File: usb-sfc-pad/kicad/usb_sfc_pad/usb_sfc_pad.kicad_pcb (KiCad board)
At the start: 2 copper layers, 36 parts, among them IC101 PIC16F1459-ISS, J101 532610671, J102 HEADER_6P-2.54, J103 532610271, J104 532610271, J105 532610271, J106 532610271, SW101 SW_Pad, SW102 SW_Pad, SW103 SW_Pad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

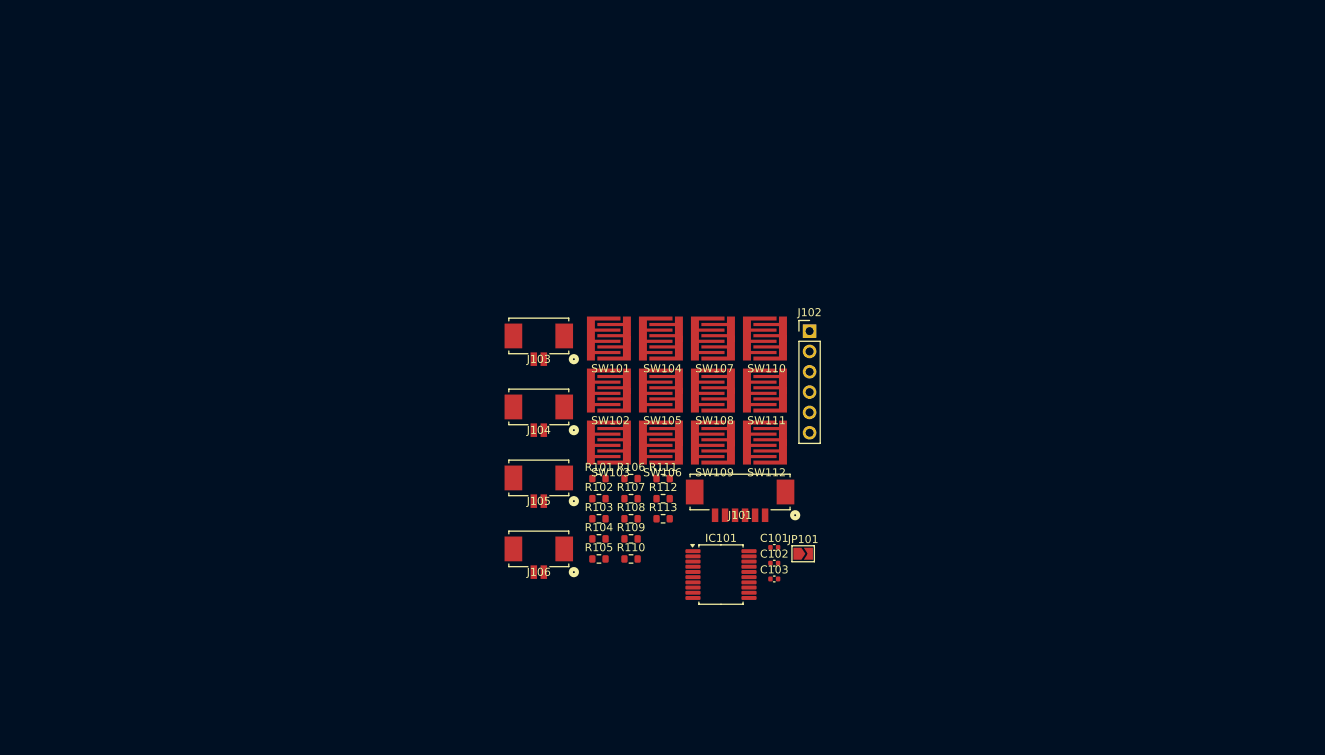
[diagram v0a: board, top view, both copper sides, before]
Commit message: Add PCB
- Renumber SFC_Pad's pins
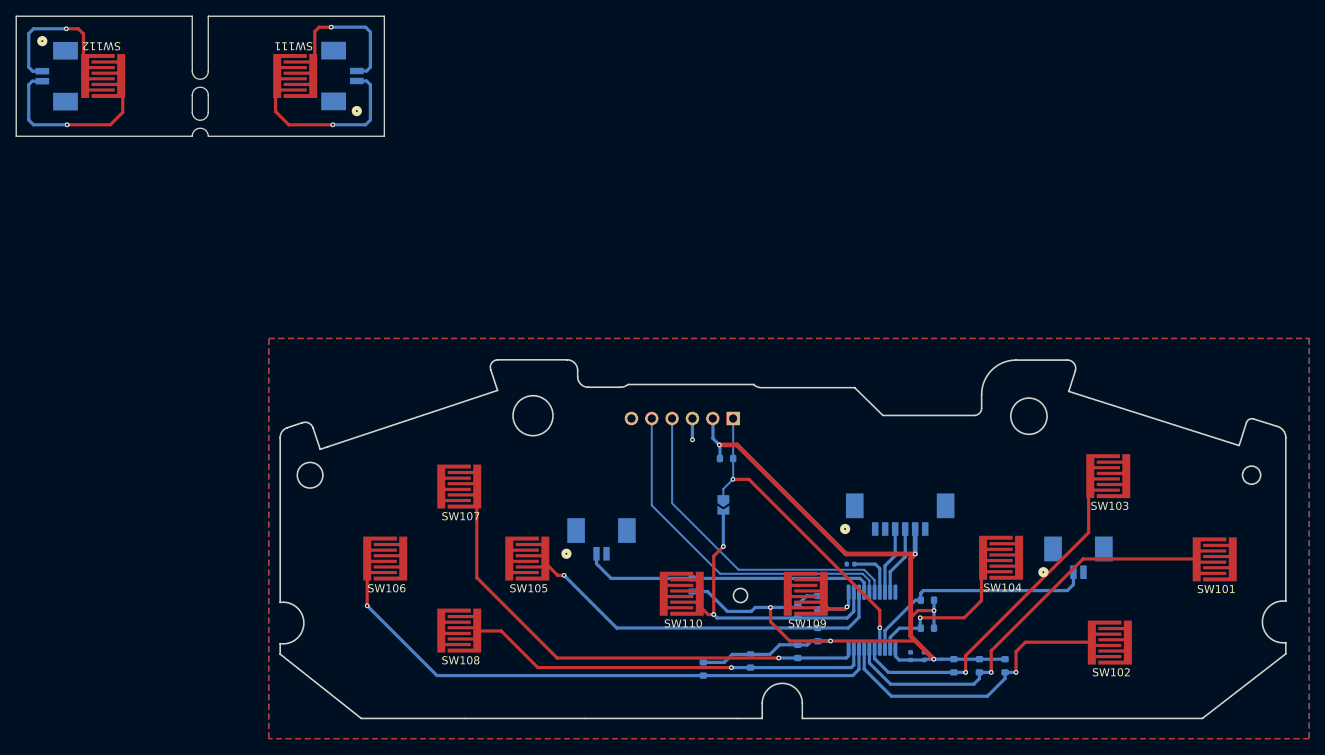
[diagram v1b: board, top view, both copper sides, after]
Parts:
- C101, C102, C103, IC101, J101, J102, J103, J104, J105, J106, JP101, R101, R102, R103, R104, R105, R106, R107, R108, R109, R110, R111, R112, R113: moved to B.Cu
- moved SW112 94.5 mm to (69.3, 47.2), turned to 180 degrees
- moved J106 83.6 mm to (64.6, 47.2), turned to 90 degrees
- moved SW101 80.6 mm to (208.2, 107.6)
- moved J103 72.5 mm to (191.2, 106.3), turned to 180 degrees
- moved SW111 70.6 mm to (93.3, 47.2), turned to 180 degrees
- moved SW102 70.1 mm to (195.1, 118.0)
- moved SW103 62.5 mm to (194.9, 97.2)
- moved R102 54.9 mm to (182.0, 120.9), turned to -90 degrees
- moved R101 53.0 mm to (178.8, 120.9), turned to -90 degrees
- moved SW104 50.6 mm to (181.5, 107.4)
- moved J104 48.7 mm to (98.1, 47.2), turned to -90 degrees
- moved R103 48.0 mm to (175.6, 120.9), turned to -90 degrees
- moved SW108 43.6 mm to (113.8, 116.5)
- moved R104 42.5 mm to (172.3, 116.2), turned to 180 degrees
- moved SW106 37.4 mm to (104.5, 107.5)
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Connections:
- IC101 pad 14: PL -> TL
- SW101 pad 1: A -> GND
- SW101 pad 2: GND -> A
- SW102 pad 1: B -> GND
- SW102 pad 2: GND -> B
- SW103 pad 1: X -> GND
- SW103 pad 2: GND -> X
- SW104 pad 1: Y -> GND
- SW104 pad 2: GND -> Y
- SW106 pad 1: LEFT -> GND
- SW106 pad 2: GND -> LEFT
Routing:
- net +5V: track 0.00 -> 133.9 mm, vias 0 -> 6
- net LEFT: track 0.00 -> 74.1 mm, vias 0 -> 1
- net UP: track 0.00 -> 63.2 mm, vias 0 -> 1
- net A: track 0.00 -> 52.2 mm, vias 0 -> 1
- net DOWN: track 0.00 -> 51.1 mm, vias 0 -> 1
- net RIGHT: track 0.00 -> 46.7 mm, vias 0 -> 1
- net X: track 0.00 -> 44.3 mm, vias 0 -> 1
- net PGC: track 0.00 -> 43.4 mm
- net PGD: track 0.00 -> 41.4 mm
- net MCLR: track 0.00 -> 40.5 mm, vias 0 -> 2
- net SELECT: track 0.00 -> 37.5 mm, vias 0 -> 2
- net B: track 0.00 -> 37.0 mm, vias 0 -> 1
- net TL: track 0.00 -> 36.9 mm
- net TR: track 0.00 -> 30.2 mm
- net Net-(J104-Pad1): track 0.00 -> 23.8 mm, vias 0 -> 1
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- added copper zone on B.Cu, net GND
- added copper zone on F.Cu, net GND
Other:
- board outline added: 158.6 x 87.8 mm

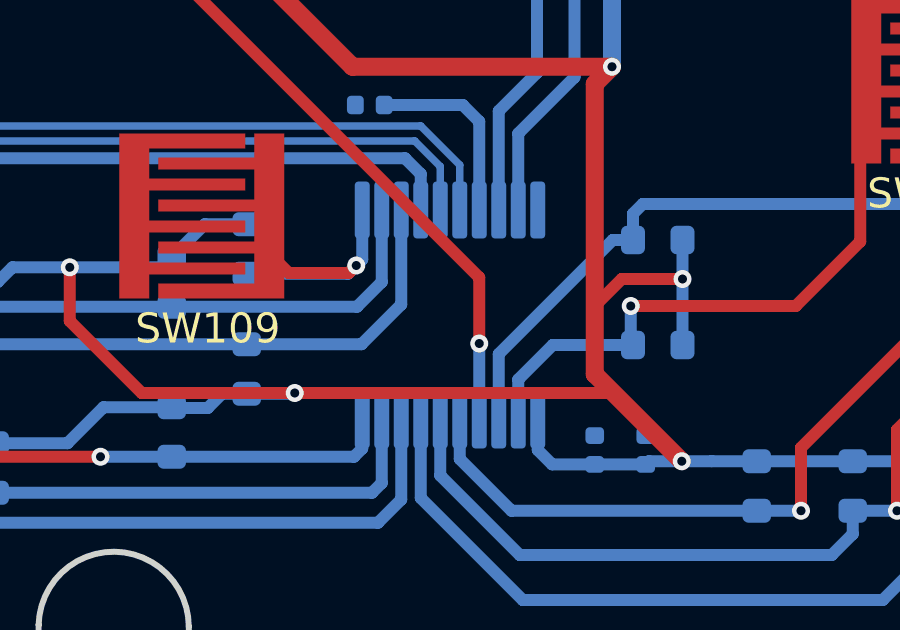
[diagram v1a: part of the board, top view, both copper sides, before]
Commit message: Fix clearance in IC101 pads
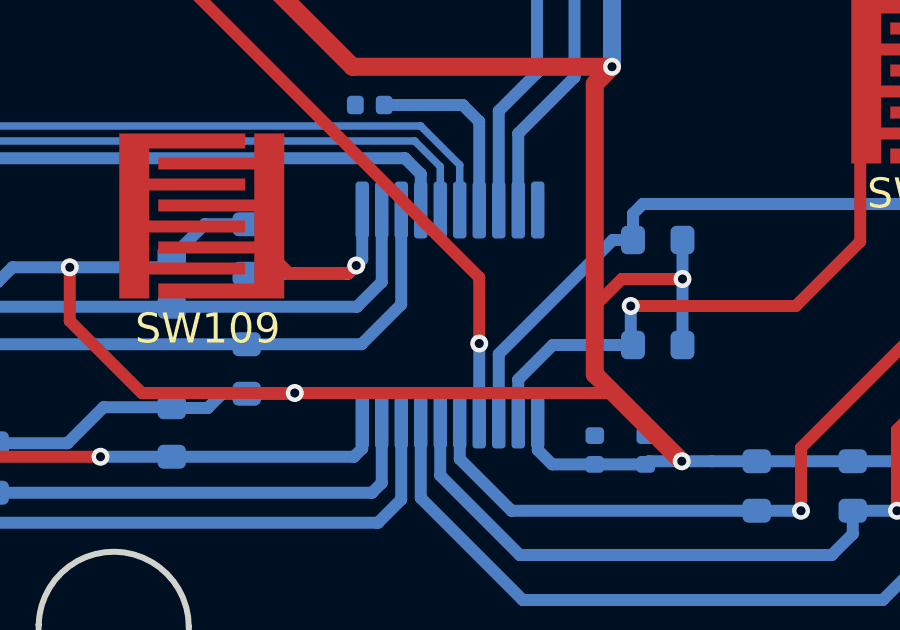
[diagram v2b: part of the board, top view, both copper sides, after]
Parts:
- IC101: footprint Package_SO:SSOP-20_5.3x7.2mm_P0.65mm -> Local:SSOP-20_5.3x7.2mm_P0.65mm
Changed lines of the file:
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@@
 		)
 	)
-	(footprint "Package_SO:SSOP-20_5.3x7.2mm_P0.65mm"
+	(footprint "Local:SSOP-20_5.3x7.2mm_P0.65mm"
 		(layer "B.Cu")
 		(at 165.375 115.2 90)
-		(descr "SSOP, 20 Pin (http://ww1.microchip.com/downloads/en/DeviceDoc/40001800C.pdf), generated with kicad-footprint-generator ipc_gullwing_generator.py")
 		(tags "SSOP SO")
 		(property "Reference" "IC101"
-			(at 0 4.55 90)
+			(at 0 4.55 -90)
 			(layer "B.SilkS")
 			(effects
@@
 		)
 		(property "Value" "PIC16F1459-ISS"
-			(at 0 -4.875 90)
+			(at 0 -4.55 -90)
 			(layer "B.Fab")
 			(effects
@@
 			)
 		)
-		(property "Footprint" "Package_SO:SSOP-20_5.3x7.2mm_P0.65mm"
-			(at 0 0 90)
+		(property "Footprint" "Local:SSOP-20_5.3x7.2mm_P0.65mm"
+			(at 0 0 -90)
 			(layer "B.Fab")
 			(hide yes)
@@
 		)
 		(property "Datasheet" "http://ww1.microchip.com/downloads/en/DeviceDoc/41639A.pdf"
-			(at 0 0 90)
+			(at 0 0 -90)
 			(layer "B.Fab")
 			(hide yes)
@@
 		)
 		(property "Description" "PIC16F1454, 8192W FLASH, 1024B SRAM, PDIP-20"
-			(at 0 0 90)
+			(at 0 0 -90)
 			(layer "B.Fab")
 			(hide yes)
@@
 		)
 		(fp_text user "${REFERENCE}"
-			(at 0 0 90)
+			(at 0 0 -90)
 			(layer "B.Fab")
 			(effects
@@
 		(pad "1" smd roundrect
 			(at -3.5 2.925 90)
-			(size 1.9 0.5)
+			(size 1.9 0.45)
 			(layers "B.Cu" "B.Paste" "B.Mask")
 			(roundrect_rratio 0.25)
@@
 		(pad "2" smd roundrect
 			(at -3.5 2.275 90)
-			(size 1.9 0.5)
+			(size 1.9 0.45)
 			(layers "B.Cu" "B.Paste" "B.Mask")
 			(roundrect_rratio 0.25)
@@
 		(pad "3" smd roundrect
 			(at -3.5 1.625 90)
-			(size 1.9 0.5)
+			(size 1.9 0.45)
 			(layers "B.Cu" "B.Paste" "B.Mask")
 			(roundrect_rratio 0.25)
@@
 		(pad "4" smd roundrect
 			(at -3.5 0.975 90)
-			(size 1.9 0.5)
+			(size 1.9 0.45)
 			(layers "B.Cu" "B.Paste" "B.Mask")
 			(roundrect_rratio 0.25)
@@
 		(pad "5" smd roundrect
 			(at -3.5 0.325 90)
-			(size 1.9 0.5)
+			(size 1.9 0.45)
 			(layers "B.Cu" "B.Paste" "B.Mask")
 			(roundrect_rratio 0.25)
@@
 		(pad "6" smd roundrect
 			(at -3.5 -0.325 90)
-			(size 1.9 0.5)
+			(size 1.9 0.45)
 			(layers "B.Cu" "B.Paste" "B.Mask")
 			(roundrect_rratio 0.25)
@@
 		(pad "7" smd roundrect
 			(at -3.5 -0.975 90)
-			(size 1.9 0.5)
+			(size 1.9 0.45)
 			(layers "B.Cu" "B.Paste" "B.Mask")
 			(roundrect_rratio 0.25)
@@
 		(pad "8" smd roundrect
 			(at -3.5 -1.625 90)
-			(size 1.9 0.5)
+			(size 1.9 0.45)
 			(layers "B.Cu" "B.Paste" "B.Mask")
 			(roundrect_rratio 0.25)
@@
 		(pad "9" smd roundrect
 			(at -3.5 -2.275 90)
-			(size 1.9 0.5)
+			(size 1.9 0.45)
 			(layers "B.Cu" "B.Paste" "B.Mask")
 			(roundrect_rratio 0.25)
@@
 		(pad "10" smd roundrect
 			(at -3.5 -2.925 90)
-			(size 1.9 0.5)
+			(size 1.9 0.45)
 			(layers "B.Cu" "B.Paste" "B.Mask")
 			(roundrect_rratio 0.25)
@@
 		(pad "11" smd roundrect
 			(at 3.5 -2.925 90)
-			(size 1.9 0.5)
+			(size 1.9 0.45)
 			(layers "B.Cu" "B.Paste" "B.Mask")
 			(roundrect_rratio 0.25)
@@
 		(pad "12" smd roundrect
 			(at 3.5 -2.275 90)
-			(size 1.9 0.5)
+			(size 1.9 0.45)
 			(layers "B.Cu" "B.Paste" "B.Mask")
 			(roundrect_rratio 0.25)
@@
 		(pad "13" smd roundrect
 			(at 3.5 -1.625 90)
-			(size 1.9 0.5)
+			(size 1.9 0.45)
 			(layers "B.Cu" "B.Paste" "B.Mask")
 			(roundrect_rratio 0.25)
@@
 		(pad "14" smd roundrect
 			(at 3.5 -0.975 90)
-			(size 1.9 0.5)
+			(size 1.9 0.45)
 			(layers "B.Cu" "B.Paste" "B.Mask")
 			(roundrect_rratio 0.25)
@@
 		(pad "15" smd roundrect
 			(at 3.5 -0.325 90)
-			(size 1.9 0.5)
+			(size 1.9 0.45)
 			(layers "B.Cu" "B.Paste" "B.Mask")
 			(roundrect_rratio 0.25)
@@
 		(pad "16" smd roundrect
 			(at 3.5 0.325 90)
-			(size 1.9 0.5)
+			(size 1.9 0.45)
 			(layers "B.Cu" "B.Paste" "B.Mask")
 			(roundrect_rratio 0.25)
@@
 		(pad "17" smd roundrect
 			(at 3.5 0.975 90)
-			(size 1.9 0.5)
+			(size 1.9 0.45)
 			(layers "B.Cu" "B.Paste" "B.Mask")
 			(roundrect_rratio 0.25)
@@
 		(pad "18" smd roundrect
 			(at 3.5 1.625 90)
-			(size 1.9 0.5)
+			(size 1.9 0.45)
 			(layers "B.Cu" "B.Paste" "B.Mask")
 			(roundrect_rratio 0.25)
@@
 		(pad "19" smd roundrect
 			(at 3.5 2.275 90)
-			(size 1.9 0.5)
+			(size 1.9 0.45)
 			(layers "B.Cu" "B.Paste" "B.Mask")
 			(roundrect_rratio 0.25)
@@
 		(pad "20" smd roundrect
 			(at 3.5 2.925 90)
-			(size 1.9 0.5)
+			(size 1.9 0.45)
 			(layers "B.Cu" "B.Paste" "B.Mask")
 			(roundrect_rratio 0.25)
@@
 			(size 1.7 1.7)
 			(drill 1)
-			(layers "*.Cu" "*.Mask" "In1.Cu" "In2.Cu" "In3.Cu" "In4.Cu" "In5.Cu" "In6.Cu"
-				"In7.Cu" "In8.Cu" "In9.Cu" "In10.Cu" "In11.Cu" "In12.Cu" "In13.Cu" "In14.Cu"
-				"In15.Cu" "In16.Cu" "In17.Cu" "In18.Cu" "In19.Cu" "In20.Cu" "In21.Cu"
-				"In22.Cu" "In23.Cu" "In24.Cu" "In25.Cu" "In26.Cu" "In27.Cu" "In28.Cu"
-				"In29.Cu" "In30.Cu"
-			)
+			(layers "*.Cu" "*.Mask")
 			(remove_unused_layers no)
 			(net 14 "MCLR")
@@
 			(size 1.7 1.7)
 			(drill 1)
-			(layers "*.Cu" "*.Mask" "In1.Cu" "In2.Cu" "In3.Cu" "In4.Cu" "In5.Cu" "In6.Cu"
-				"In7.Cu" "In8.Cu" "In9.Cu" "In10.Cu" "In11.Cu" "In12.Cu" "In13.Cu" "In14.Cu"
-				"In15.Cu" "In16.Cu" "In17.Cu" "In18.Cu" "In19.Cu" "In20.Cu" "In21.Cu"
-				"In22.Cu" "In23.Cu" "In24.Cu" "In25.Cu" "In26.Cu" "In27.Cu" "In28.Cu"
-				"In29.Cu" "In30.Cu"
-			)
+			(layers "*.Cu" "*.Mask")
 			(remove_unused_layers no)
 			(net 2 "+5V")
@@
 			(size 1.7 1.7)
 			(drill 1)
-			(layers "*.Cu" "*.Mask" "In1.Cu" "In2.Cu" "In3.Cu" "In4.Cu" "In5.Cu" "In6.Cu"
-				"In7.Cu" "In8.Cu" "In9.Cu" "In10.Cu" "In11.Cu" "In12.Cu" "In13.Cu" "In14.Cu"
-				"In15.Cu" "In16.Cu" "In17.Cu" "In18.Cu" "In19.Cu" "In20.Cu" "In21.Cu"
-				"In22.Cu" "In23.Cu" "In24.Cu" "In25.Cu" "In26.Cu" "In27.Cu" "In28.Cu"
-				"In29.Cu" "In30.Cu"
-			)
+			(layers "*.Cu" "*.Mask")
 			(remove_unused_layers no)
 			(net 1 "GND")
@@
 			(size 1.7 1.7)
 			(drill 1)
-			(layers "*.Cu" "*.Mask" "In1.Cu" "In2.Cu" "In3.Cu" "In4.Cu" "In5.Cu" "In6.Cu"
-				"In7.Cu" "In8.Cu" "In9.Cu" "In10.Cu" "In11.Cu" "In12.Cu" "In13.Cu" "In14.Cu"
-				"In15.Cu" "In16.Cu" "In17.Cu" "In18.Cu" "In19.Cu" "In20.Cu" "In21.Cu"
-				"In22.Cu" "In23.Cu" "In24.Cu" "In25.Cu" "In26.Cu" "In27.Cu" "In28.Cu"
-				"In29.Cu" "In30.Cu"
-			)
+			(layers "*.Cu" "*.Mask")
 			(remove_unused_layers no)
 			(net 18 "PGD")
@@
 			(size 1.7 1.7)
 			(drill 1)
-			(layers "*.Cu" "*.Mask" "In1.Cu" "In2.Cu" "In3.Cu" "In4.Cu" "In5.Cu" "In6.Cu"
-				"In7.Cu" "In8.Cu" "In9.Cu" "In10.Cu" "In11.Cu" "In12.Cu" "In13.Cu" "In14.Cu"
-				"In15.Cu" "In16.Cu" "In17.Cu" "In18.Cu" "In19.Cu" "In20.Cu" "In21.Cu"
-				"In22.Cu" "In23.Cu" "In24.Cu" "In25.Cu" "In26.Cu" "In27.Cu" "In28.Cu"
-				"In29.Cu" "In30.Cu"
-			)
+			(layers "*.Cu" "*.Mask")
 			(remove_unused_layers no)
 			(net 13 "PGC")
@@
 			(size 1.7 1.7)
 			(drill 1)
-			(layers "*.Cu" "*.Mask" "In1.Cu" "In2.Cu" "In3.Cu" "In4.Cu" "In5.Cu" "In6.Cu"
-				"In7.Cu" "In8.Cu" "In9.Cu" "In10.Cu" "In11.Cu" "In12.Cu" "In13.Cu" "In14.Cu"
-				"In15.Cu" "In16.Cu" "In17.Cu" "In18.Cu" "In19.Cu" "In20.Cu" "In21.Cu"
-				"In22.Cu" "In23.Cu" "In24.Cu" "In25.Cu" "In26.Cu" "In27.Cu" "In28.Cu"
-				"In29.Cu" "In30.Cu"
-			)
+			(layers "*.Cu" "*.Mask")
 			(remove_unused_layers no)
 			(net 21 "unconnected-(J102-Pin_6-Pad6)")
